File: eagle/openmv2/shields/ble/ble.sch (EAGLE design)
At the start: 20 parts, among them U2 OPENMV3

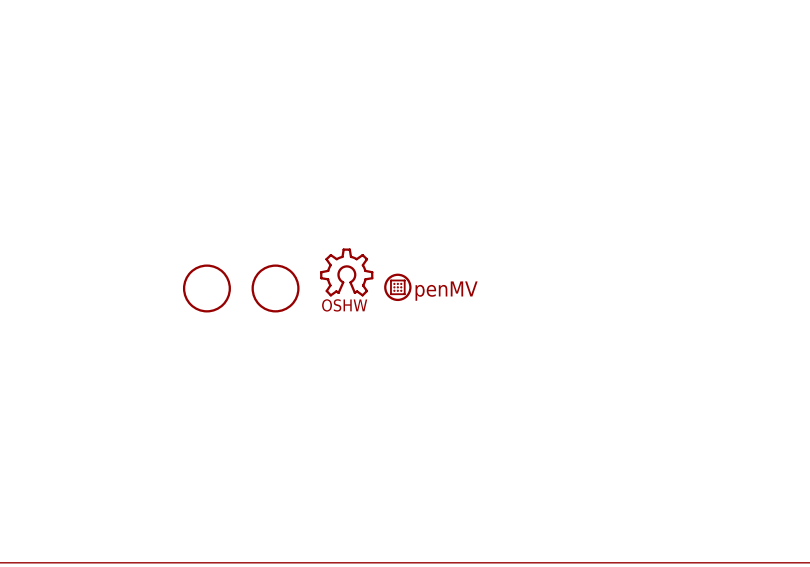
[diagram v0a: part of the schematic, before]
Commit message: Update shields silk-screen.
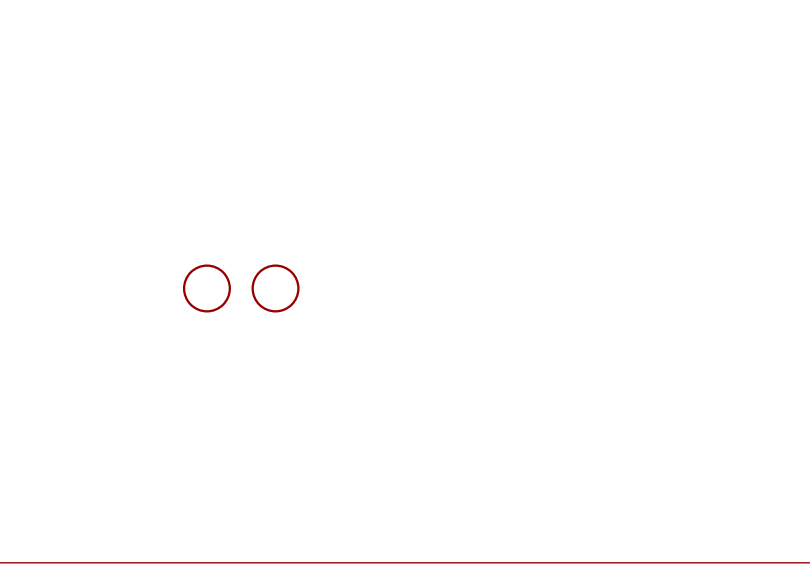
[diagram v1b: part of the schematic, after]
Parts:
- removed LOGO1: OSHW_LOGO_6MILX0150-NT, iofault:OSHW_LOGO_6MILX0150-NT
- removed U$4: OPENMV-LOGO, openmv:OPENMV-LOGO
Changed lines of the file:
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@@
 <grid distance="0.1" unitdist="inch" unit="inch" style="lines" multiple="1" display="no" altdistance="0.01" altunitdist="inch" altunit="inch"/>
 <layers>
-<layer number="1" name="Top" color="4" fill="1" visible="yes" active="no"/>
-<layer number="2" name="Route2" color="1" fill="3" visible="yes" active="no"/>
-<layer number="3" name="Route3" color="4" fill="3" visible="yes" active="no"/>
-<layer number="4" name="Route4" color="1" fill="4" visible="yes" active="no"/>
-<layer number="5" name="Route5" color="4" fill="4" visible="yes" active="no"/>
-<layer number="6" name="Route6" color="1" fill="8" visible="yes" active="no"/>
-<layer number="7" name="Route7" color="4" fill="8" visible="yes" active="no"/>
-<layer number="8" name="Route8" color="1" fill="2" visible="yes" active="no"/>
-<layer number="9" name="Route9" color="4" fill="2" visible="yes" active="no"/>
-<layer number="10" name="Route10" color="1" fill="7" visible="yes" active="no"/>
-<layer number="11" name="Route11" color="4" fill="7" visible="yes" active="no"/>
-<layer number="12" name="Route12" color="1" fill="5" visible="yes" active="no"/>
-<layer number="13" name="Route13" color="4" fill="5" visible="yes" active="no"/>
-<layer number="14" name="Route14" color="1" fill="6" visible="yes" active="no"/>
-<layer number="15" name="Route15" color="4" fill="1" visible="yes" active="no"/>
-<layer number="16" name="Bottom" color="1" fill="1" visible="yes" active="no"/>
-<layer number="17" name="Pads" color="2" fill="1" visible="yes" active="no"/>
-<layer number="18" name="Vias" color="2" fill="1" visible="yes" active="no"/>
-<layer number="19" name="Unrouted" color="6" fill="1" visible="yes" active="no"/>
-<layer number="20" name="Dimension" color="15" fill="1" visible="yes" active="no"/>
-<layer number="21" name="tPlace" color="7" fill="1" visible="yes" active="no"/>
-<layer number="22" name="bPlace" color="7" fill="1" visible="yes" active="no"/>
-<layer number="23" name="tOrigins" color="15" fill="1" visible="yes" active="no"/>
-<layer number="24" name="bOrigins" color="15" fill="1" visible="yes" active="no"/>
-<layer number="25" name="tNames" color="7" fill="1" visible="yes" active="no"/>
-<layer number="26" name="bNames" color="7" fill="1" visible="yes" active="no"/>
-<layer number="27" name="tValues" color="7" fill="1" visible="yes" active="no"/>
-<layer number="28" name="bValues" color="7" fill="1" visible="yes" active="no"/>
+<layer number="1" name="Top" color="4" fill="1" visible="no" active="no"/>
+<layer number="2" name="Route2" color="1" fill="3" visible="no" active="no"/>
+<layer number="3" name="Route3" color="4" fill="3" visible="no" active="no"/>
+<layer number="4" name="Route4" color="1" fill="4" visible="no" active="no"/>
+<layer number="5" name="Route5" color="4" fill="4" visible="no" active="no"/>
+<layer number="6" name="Route6" color="1" fill="8" visible="no" active="no"/>
+<layer number="7" name="Route7" color="4" fill="8" visible="no" active="no"/>
+<layer number="8" name="Route8" color="1" fill="2" visible="no" active="no"/>
+<layer number="9" name="Route9" color="4" fill="2" visible="no" active="no"/>
+<layer number="10" name="Route10" color="1" fill="7" visible="no" active="no"/>
+<layer number="11" name="Route11" color="4" fill="7" visible="no" active="no"/>
+<layer number="12" name="Route12" color="1" fill="5" visible="no" active="no"/>
+<layer number="13" name="Route13" color="4" fill="5" visible="no" active="no"/>
+<layer number="14" name="Route14" color="1" fill="6" visible="no" active="no"/>
+<layer number="15" name="Route15" color="4" fill="1" visible="no" active="no"/>
+<layer number="16" name="Bottom" color="1" fill="1" visible="no" active="no"/>
+<layer number="17" name="Pads" color="2" fill="1" visible="no" active="no"/>
+<layer number="18" name="Vias" color="2" fill="1" visible="no" active="no"/>
+<layer number="19" name="Unrouted" color="6" fill="1" visible="no" active="no"/>
+<layer number="20" name="Dimension" color="15" fill="1" visible="no" active="no"/>
+<layer number="21" name="tPlace" color="7" fill="1" visible="no" active="no"/>
+<layer number="22" name="bPlace" color="7" fill="1" visible="no" active="no"/>
+<layer number="23" name="tOrigins" color="15" fill="1" visible="no" active="no"/>
+<layer number="24" name="bOrigins" color="15" fill="1" visible="no" active="no"/>
+<layer number="25" name="tNames" color="7" fill="1" visible="no" active="no"/>
+<layer number="26" name="bNames" color="7" fill="1" visible="no" active="no"/>
+<layer number="27" name="tValues" color="7" fill="1" visible="no" active="no"/>
+<layer number="28" name="bValues" color="7" fill="1" visible="no" active="no"/>
 <layer number="29" name="tStop" color="7" fill="3" visible="no" active="no"/>
 <layer number="30" name="bStop" color="7" fill="6" visible="no" active="no"/>
@@
 <layer number="35" name="tGlue" color="7" fill="4" visible="no" active="no"/>
 <layer number="36" name="bGlue" color="7" fill="5" visible="no" active="no"/>
-<layer number="37" name="tTest" color="7" fill="1" visible="yes" active="no"/>
-<layer number="38" name="bTest" color="7" fill="1" visible="yes" active="no"/>
+<layer number="37" name="tTest" color="7" fill="1" visible="no" active="no"/>
+<layer number="38" name="bTest" color="7" fill="1" visible="no" active="no"/>
 <layer number="39" name="tKeepout" color="4" fill="11" visible="no" active="no"/>
 <layer number="40" name="bKeepout" color="1" fill="11" visible="no" active="no"/>
@@
 <layer number="44" name="Drills" color="7" fill="1" visible="no" active="no"/>
 <layer number="45" name="Holes" color="7" fill="1" visible="no" active="no"/>
-<layer number="46" name="Milling" color="3" fill="1" visible="yes" active="no"/>
-<layer number="47" name="Measures" color="7" fill="1" visible="yes" active="no"/>
-<layer number="48" name="Document" color="7" fill="1" visible="yes" active="no"/>
-<layer number="49" name="Reference" color="7" fill="1" visible="yes" active="no"/>
-<layer number="50" name="dxf" color="7" fill="1" visible="yes" active="no"/>
-<layer number="51" name="tDocu" color="7" fill="1" visible="yes" active="no"/>
-<layer number="52" name="bDocu" color="7" fill="1" visible="yes" active="no"/>
-<layer number="53" name="tGND_GNDA" color="7" fill="9" visible="yes" active="no"/>
-<layer number="54" name="bGND_GNDA" color="1" fill="9" visible="yes" active="no"/>
-<layer number="56" name="wert" color="7" fill="1" visible="yes" active="no"/>
-<layer number="57" name="tCAD" color="7" fill="1" visible="yes" active="no"/>
-<layer number="59" name="Invisible" color="7" fill="1" visible="yes" active="no"/>
-<layer number="61" name="stand" color="7" fill="1" visible="yes" active="no"/>
+<layer number="46" name="Milling" color="3" fill="1" visible="no" active="no"/>
+<layer number="47" name="Measures" color="7" fill="1" visible="no" active="no"/>
+<layer number="48" name="Document" color="7" fill="1" visible="no" active="no"/>
+<layer number="49" name="Reference" color="7" fill="1" visible="no" active="no"/>
+<layer number="50" name="dxf" color="7" fill="1" visible="no" active="no"/>
+<layer number="51" name="tDocu" color="7" fill="1" visible="no" active="no"/>
+<layer number="52" name="bDocu" color="7" fill="1" visible="no" active="no"/>
+<layer number="53" name="tGND_GNDA" color="7" fill="9" visible="no" active="no"/>
+<layer number="54" name="bGND_GNDA" color="1" fill="9" visible="no" active="no"/>
+<layer number="56" name="wert" color="7" fill="1" visible="no" active="no"/>
+<layer number="57" name="tCAD" color="7" fill="1" visible="no" active="no"/>
+<layer number="59" name="Invisible" color="7" fill="1" visible="no" active="no"/>
+<layer number="61" name="stand" color="7" fill="1" visible="no" active="no"/>
 <layer number="91" name="Nets" color="2" fill="1" visible="yes" active="yes"/>
 <layer number="92" name="Busses" color="1" fill="1" visible="yes" active="yes"/>
@@
 <attribute name="TP_SIGNAL_NAME" value=""/>
 </part>
-<part name="U$4" library="openmv" deviceset="OPENMV-LOGO" device=""/>
-<part name="LOGO1" library="iofault" deviceset="OSHW_LOGO_6MIL" device="X0150-NT"/>
 <part name="U$3" library="AMS" deviceset="AMS00X" device=""/>
 <part name="GND3" library="supply1" deviceset="GND" device=""/>
@@
 <attribute name="TP_SIGNAL_NAME" x="64.77" y="130.81" size="1.778" layer="97" rot="R90"/>
 </instance>
-<instance part="U$4" gate="G$1" x="304.8" y="30.48"/>
-<instance part="LOGO1" gate="G$1" x="292.1" y="27.94"/>
 <instance part="U$3" gate="G$1" x="114.3" y="121.92"/>
 <instance part="GND3" gate="1" x="55.88" y="73.66"/>
